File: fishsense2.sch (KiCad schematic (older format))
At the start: 20 parts, among them J1 Conn_02x10_Odd_Even, J2 Screw_Terminal_01x02, J3 Conn_01x02, J4 Conn_01x02, J5 Conn_01x02, J6 USB_C_Receptacle, J7 USB_C_Receptacle, J8 USB_C_Receptacle, K1 ADW11, U1 P783F-Q24-S5-S, U2 AD9951

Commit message: Added symbols and footprints. More space for connectors on PCB.
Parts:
- removed J7, J8: USB_C_Receptacle, Connector_USB:USB_C_Receptacle_GCT_USB4085, symbol Connector:USB_C_Receptacle
- removed U2: AD9951, Package_QFP:TQFP-48-1EP_7x7mm_P0.5mm_EP3.5x3.5mm, symbol Interface:AD9951
- added J7, J8: USB3_A, Connector_USB:USB3_A_Molex_48393-001, symbol Connector:USB3_A
- added U2: TUSB8020BIPHP, fishsense2:TUSB8020BIPHP, symbol New_Library:TUSB8020BIPHP
- added U3: HD3SS3220, fishsense2:TI_VQFN_RNH, symbol New_Library:HD3SS3220
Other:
- moved on the sheet: J3, U1
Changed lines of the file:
@@
 $EndDescr
-$Comp
-L Interface:AD9951 U2
-U 1 1 6166350E
-P 4450 3650
-F 0 "U2" H 5594 3696 50  0000 L CNN
-F 1 "AD9951" H 5594 3605 50  0000 L CNN
-F 2 "Package_QFP:TQFP-48-1EP_7x7mm_P0.5mm_EP3.5x3.5mm" H 4450 2450 50  0001 C CIN
-F 3 "https://www.analog.com/static/imported-files/data_sheets/AD9951.pdf" H 4450 3650 50  0001 C CNN
-	1    4450 3650
-	1    0    0    -1
-$EndComp
-$Comp
-L Connector:USB_C_Receptacle J8
-U 1 1 61664802
-P 9700 2150
-F 0 "J8" H 9807 3417 50  0000 C CNN
-F 1 "USB_C_Receptacle" H 9807 3326 50  0000 C CNN
-F 2 "Connector_USB:USB_C_Receptacle_GCT_USB4085" H 9850 2150 50  0001 C CNN
-F 3 "https://www.usb.org/sites/default/files/documents/usb_type-c.zip" H 9850 2150 50  0001 C CNN
-	1    9700 2150
-	1    0    0    -1
-$EndComp
-$Comp
-L Connector:USB_C_Receptacle J7
-U 1 1 61667CF7
-P 9650 5100
-F 0 "J7" H 9757 6367 50  0000 C CNN
-F 1 "USB_C_Receptacle" H 9757 6276 50  0000 C CNN
-F 2 "Connector_USB:USB_C_Receptacle_GCT_USB4085" H 9800 5100 50  0001 C CNN
-F 3 "https://www.usb.org/sites/default/files/documents/usb_type-c.zip" H 9800 5100 50  0001 C CNN
-	1    9650 5100
-	1    0    0    -1
-$EndComp
-$Comp
-L Connector:USB_C_Receptacle J6
-U 1 1 6166A7B3
-P 8400 5100
-F 0 "J6" H 8507 6367 50  0000 C CNN
-F 1 "USB_C_Receptacle" H 8507 6276 50  0000 C CNN
-F 2 "Connector_USB:USB_C_Receptacle_GCT_USB4085" H 8550 5100 50  0001 C CNN
-F 3 "https://www.usb.org/sites/default/files/documents/usb_type-c.zip" H 8550 5100 50  0001 C CNN
-	1    8400 5100
-	1    0    0    -1
-$EndComp
 $Comp
 L Device:LED D1
@@
 L New_Library:P783F-Q24-S5-S U1
 U 1 1 616833DA
-P 1850 4100
-F 0 "U1" H 2075 4225 50  0000 C CNN
-F 1 "P783F-Q24-S5-S" H 2075 4134 50  0000 C CNN
-F 2 "Converter_DCDC:Converter_DCDC_RECOM_R5xxxPA_THT" H 1850 4100 50  0001 C CNN
-F 3 "" H 1850 4100 50  0001 C CNN
-	1    1850 4100
+P 4750 6050
+F 0 "U1" H 4975 6175 50  0000 C CNN
+F 1 "P783F-Q24-S5-S" H 4975 6084 50  0000 C CNN
+F 2 "Converter_DCDC:Converter_DCDC_RECOM_R5xxxPA_THT" H 4750 6050 50  0001 C CNN
+F 3 "" H 4750 6050 50  0001 C CNN
+	1    4750 6050
 	1    0    0    -1
 $EndComp
@@
 L Relay:ADW11 K1
 U 1 1 6168A988
-P 2800 6200
-F 0 "K1" H 3230 6246 50  0000 L CNN
-F 1 "ADW11" H 3230 6155 50  0000 L CNN
-F 2 "Relay_THT:Relay_SPST_TE_PCN-1xxD3MHZ" H 4125 6150 50  0001 C CNN
-F 3 "https://www.panasonic-electric-works.com/pew/es/downloads/ds_dw_hl_en.pdf" H 2800 6200 50  0001 C CNN
-	1    2800 6200
+P 2250 6900
+F 0 "K1" H 2680 6946 50  0000 L CNN
+F 1 "ADW11" H 2680 6855 50  0000 L CNN
+F 2 "Relay_THT:Relay_SPST_TE_PCN-1xxD3MHZ" H 3575 6850 50  0001 C CNN
+F 3 "https://www.panasonic-electric-works.com/pew/es/downloads/ds_dw_hl_en.pdf" H 2250 6900 50  0001 C CNN
+	1    2250 6900
 	1    0    0    -1
 $EndComp
@@
 L Connector_Generic:Conn_01x02 J3
 U 1 1 616936C7
-P 3150 1900
-F 0 "J3" H 3230 1892 50  0000 L CNN
-F 1 "Conn_01x02" H 3230 1801 50  0000 L CNN
-F 2 "Connector_AMASS:AMASS_XT30U-F_1x02_P5.0mm_Vertical" H 3150 1900 50  0001 C CNN
-F 3 "~" H 3150 1900 50  0001 C CNN
-	1    3150 1900
+P 2950 1650
+F 0 "J3" H 3030 1642 50  0000 L CNN
+F 1 "Conn_01x02" H 3030 1551 50  0000 L CNN
+F 2 "Connector_AMASS:AMASS_XT30U-F_1x02_P5.0mm_Vertical" H 2950 1650 50  0001 C CNN
+F 3 "~" H 2950 1650 50  0001 C CNN
+	1    2950 1650
 	1    0    0    -1
 $EndComp
@@
 	1    0    0    -1
 $EndComp
+$Comp
+L Connector:USB3_A J7
+U 1 1 616E2E2E
+P 9650 2550
+F 0 "J7" H 9707 3267 50  0000 C CNN
+F 1 "USB3_A" H 9707 3176 50  0000 C CNN
+F 2 "Connector_USB:USB3_A_Molex_48393-001" H 9800 2650 50  0001 C CNN
+F 3 "~" H 9800 2650 50  0001 C CNN
+	1    9650 2550
+	1    0    0    -1
+$EndComp
+$Comp
+L Connector:USB3_A J8
+U 1 1 616E6C04
+P 9650 4300
+F 0 "J8" H 9707 5017 50  0000 C CNN
+F 1 "USB3_A" H 9707 4926 50  0000 C CNN
+F 2 "Connector_USB:USB3_A_Molex_48393-001" H 9800 4400 50  0001 C CNN
+F 3 "~" H 9800 4400 50  0001 C CNN
+	1    9650 4300
+	1    0    0    -1
+$EndComp
+$Comp
+L New_Library:HD3SS3220 U3
+U 1 1 61711409
+P 7500 4600
+F 0 "U3" H 7500 5615 50  0000 C CNN
+F 1 "HD3SS3220" H 7500 5524 50  0000 C CNN
+F 2 "fishsense2:TI_VQFN_RNH" H 7500 5550 50  0001 C CNN
+F 3 "" H 7500 5550 50  0001 C CNN
+	1    7500 4600
+	1    0    0    -1
+$EndComp
+$Comp
+L New_Library:TUSB8020BIPHP U2
+U 1 1 61718548
+P 4000 3900
+F 0 "U2" H 4000 5888 60  0000 C CNN
+F 1 "TUSB8020BIPHP" H 4000 5782 60  0000 C CNN
+F 2 "fishsense2:TUSB8020BIPHP" H 4000 4140 60  0001 C CNN
+F 3 "" H 3800 5700 60  0000 C CNN
+	1    4000 3900
+	1    0    0    -1
+$EndComp
+$Comp
+L Connector:USB_C_Receptacle J6
+U 1 1 6172C2EF
+P 1100 4900
+F 0 "J6" H 1207 6167 50  0000 C CNN
+F 1 "USB_C_Receptacle" H 1207 6076 50  0000 C CNN
+F 2 "Connector_USB:USB_C_Receptacle_GCT_USB4085" H 1250 4900 50  0001 C CNN
+F 3 "https://www.usb.org/sites/default/files/documents/usb_type-c.zip" H 1250 4900 50  0001 C CNN
+	1    1100 4900
+	1    0    0    -1
+$EndComp

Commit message: Finished schematic. Added all footprints. Arranged components and routed differential signals.
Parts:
- removed D2, D3, D4: LED, LED_THT:LED_D5.0mm_FlatTop, symbol Device:LED
- removed F1: Fuse, Fuse:Fuseholder_Cylinder-5x20mm_Stelvio-Kontek_PTF78_Horizontal_Open, symbol Device:Fuse
- removed J2: Screw_Terminal_01x02, TerminalBlock:TerminalBlock_Altech_AK300-2_P5.00mm, symbol Connector:Screw_Terminal_01x02
- removed J3: Conn_01x02, Connector_AMASS:AMASS_XT30U-F_1x02_P5.0mm_Vertical, symbol Connector_Generic:Conn_01x02
- removed J4, J5: Conn_01x02, Connector_PinHeader_2.54mm:PinHeader_1x02_P2.54mm_Vertical, symbol Connector_Generic:Conn_01x02
- removed K1: ADW11, Relay_THT:Relay_SPST_TE_PCN-1xxD3MHZ, symbol Relay:ADW11
- removed U1: P783F-Q24-S5-S, Converter_DCDC:Converter_DCDC_RECOM_R5xxxPA_THT, symbol New_Library:P783F-Q24-S5-S
- added C1, C4: 18p, Capacitor_SMD:C_0603_1608Metric, symbol Device:C
- added C10, C12, C13, C14, C15, C21: 100n, Capacitor_SMD:C_0402_1005Metric, symbol Device:C
- added C11, C16, C17, C19, C2, C20, C22, C23, C3, C35, C36, C37, C38, C5, C6, C7, C8, C9: 0.1u, Capacitor_SMD:C_0402_1005Metric, symbol Device:C
- added C18: 10u, Capacitor_SMD:C_1206_3216Metric, symbol Device:C
- added C24: 100u, Capacitor_THT:CP_Radial_D5.0mm_P2.00mm, symbol Device:CP1
- added C25: 1u, Capacitor_SMD:C_1206_3216Metric, symbol Device:C
- added Q1: Q_NMOS_DGS, Package_TO_SOT_SMD:SOT-23, symbol Device:Q_NMOS_DGS
- added R1: 1M, Resistor_SMD:R_0603_1608Metric, symbol Device:R_US
- added R2: 90k, Resistor_SMD:R_0603_1608Metric, symbol Device:R_US
- added R3: 10k, Resistor_SMD:R_0603_1608Metric, symbol Device:R_US
- added R4: 9k53, Resistor_SMD:R_0603_1608Metric, symbol Device:R_US
- added R5: 200k, Resistor_SMD:R_0603_1608Metric, symbol Device:R_US
- added R6: 4.7k, Resistor_SMD:R_0603_1608Metric, symbol Device:R_US
- added R7: 900k, Resistor_SMD:R_0603_1608Metric, symbol Device:R_US
- added R8: 1k, Resistor_SMD:R_0603_1608Metric, symbol Device:R_US
- added R9: 220, Resistor_SMD:R_0603_1608Metric, symbol Device:R_US
- added SW1: SW_Reed, Connector_JST:JST_PH_B2B-PH-K_1x02_P2.00mm_Vertical, symbol Switch:SW_Reed
- added TP1: CC1, TestPoint:TestPoint_Pad_1.5x1.5mm, symbol Connector:TestPoint
- added TP2: CC2, TestPoint:TestPoint_Pad_1.5x1.5mm, symbol Connector:TestPoint
- added Y1: Crystal, Crystal:Crystal_SMD_0603-2Pin_6.0x3.5mm, symbol Device:Crystal
- J6: footprint Connector_USB:USB_C_Receptacle_GCT_USB4085 -> Connector_USB:USB_C_Receptacle_JAE_DX07S024WJ1R350
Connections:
- net labels added: +3.3V, +5V, CC1, CC2, D_DN1_N, D_DN1_P, D_DN2_N, D_DN2_P, D_UP_N, D_UP_P, GND, REED, RELAY_CTL, RX1_N, RX1_P, RX2_N, RX2_P, RX_DN1_N, RX_DN1_P, RX_DN2_N, RX_DN2_P, RX_N, RX_P, TX1_F_N, TX1_F_P, TX1_N, TX1_P, TX2_F_N, TX2_F_P, TX2_N, TX2_P, TX_DN1_F_N, TX_DN1_F_P, TX_DN1_N, TX_DN1_P, TX_DN2_F_N, TX_DN2_F_P, TX_DN2_N, TX_DN2_P, TX_N, TX_P, VBUS_UP, XI, XO
- wire segments 0 -> 241
- no-connect marks 0 -> 30
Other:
- note added: "Orbitty Connector"
- note added: "USB Hub"
- note added: "USB Receptacles"
- moved on the sheet: D1, H1, H2, H3, H4, J1, J7, J8

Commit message: Updated footprints. Placed components and added silkscreen.
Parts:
- removed C1, C4: 18p, Capacitor_SMD:C_0603_1608Metric, symbol Device:C
- removed C10, C12, C13, C14, C15, C21: 100n, Capacitor_SMD:C_0402_1005Metric, symbol Device:C
- removed C11, C16, C17, C19, C2, C20, C22, C23, C3, C35, C36, C37, C38, C5, C6, C7, C8, C9: 0.1u, Capacitor_SMD:C_0402_1005Metric, symbol Device:C
- removed C18: 10u, Capacitor_SMD:C_1206_3216Metric, symbol Device:C
- removed C24: 100u, Capacitor_THT:CP_Radial_D5.0mm_P2.00mm, symbol Device:CP1
- removed C25: 1u, Capacitor_SMD:C_1206_3216Metric, symbol Device:C
- removed J6: USB_C_Receptacle, Connector_USB:USB_C_Receptacle_JAE_DX07S024WJ1R350, symbol Connector:USB_C_Receptacle
- removed R1: 1M, Resistor_SMD:R_0603_1608Metric, symbol Device:R_US
- removed R2: 90k, Resistor_SMD:R_0603_1608Metric, symbol Device:R_US
- removed R3: 10k, Resistor_SMD:R_0603_1608Metric, symbol Device:R_US
- removed R4: 9k53, Resistor_SMD:R_0603_1608Metric, symbol Device:R_US
- removed R5: 200k, Resistor_SMD:R_0603_1608Metric, symbol Device:R_US
- removed R6: 4.7k, Resistor_SMD:R_0603_1608Metric, symbol Device:R_US
- removed R7: 900k, Resistor_SMD:R_0603_1608Metric, symbol Device:R_US
- removed R8: 1k, Resistor_SMD:R_0603_1608Metric, symbol Device:R_US
- removed TP1: CC1, TestPoint:TestPoint_Pad_1.5x1.5mm, symbol Connector:TestPoint
- removed TP2: CC2, TestPoint:TestPoint_Pad_1.5x1.5mm, symbol Connector:TestPoint
- removed U2: TUSB8020BIPHP, fishsense2:TUSB8020BIPHP, symbol New_Library:TUSB8020BIPHP
- removed U3: HD3SS3220, fishsense2:TI_VQFN_RNH, symbol New_Library:HD3SS3220
- removed Y1: Crystal, Crystal:Crystal_SMD_0603-2Pin_6.0x3.5mm, symbol Device:Crystal
- added J10: USB_B_Micro, Connector_USB:USB_Micro-B_GCT_USB3076-30-A, symbol Connector:USB_B_Micro
- added J5, J6: USB3_A, Connector_USB:USB3_A_Molex_48393-001, symbol Connector:USB3_A
- added J9: Barrel_Jack, Connector_BarrelJack:BarrelJack_Horizontal, symbol Connector:Barrel_Jack
- R9: footprint Resistor_SMD:R_0603_1608Metric -> Resistor_SMD:R_1206_3216Metric_Pad1.30x1.75mm_HandSolder
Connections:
- net labels removed: +3.3V, +5V, CC1, CC2, D_DN1_N, D_DN1_P, D_DN2_N, D_DN2_P, D_UP_N, D_UP_P, RX1_N, RX1_P, RX2_N, RX2_P, RX_DN1_N, RX_DN1_P, RX_DN2_N, RX_DN2_P, RX_N, RX_P, TX1_F_N, TX1_F_P, TX1_N, TX1_P, TX2_F_N, TX2_F_P, TX2_N, TX2_P, TX_DN1_F_N, TX_DN1_F_P, TX_DN1_N, TX_DN1_P, TX_DN2_F_N, TX_DN2_F_P, TX_DN2_N, TX_DN2_P, TX_N, TX_P, VBUS_UP, XI, XO
- wire segments 241 -> 14
- no-connect marks 30 -> 11
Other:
- note removed: "USB Hub"
- note removed: "USB Receptacles"
- moved on the sheet: D1, H1, H2, H3, H4, J1, Q1, R9, SW1

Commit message: Changed footprints to right angle versions. Adjusted board outline to orbitty carrier size.
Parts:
- SW1: footprint Connector_JST:JST_PH_B2B-PH-K_1x02_P2.00mm_Vertical -> Connector_JST:JST_PH_S2B-PH-K_1x02_P2.00mm_Horizontal
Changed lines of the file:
@@
 F 0 "SW1" V 1896 4365 50  0000 R CNN
 F 1 "SW_Reed" V 1805 4365 50  0000 R CNN
-F 2 "Connector_JST:JST_PH_B2B-PH-K_1x02_P2.00mm_Vertical" H 1850 4450 50  0001 C CNN
+F 2 "Connector_JST:JST_PH_S2B-PH-K_1x02_P2.00mm_Horizontal" H 1850 4450 50  0001 C CNN
 F 3 "~" H 1850 4450 50  0001 C CNN
 	1    1850 4450

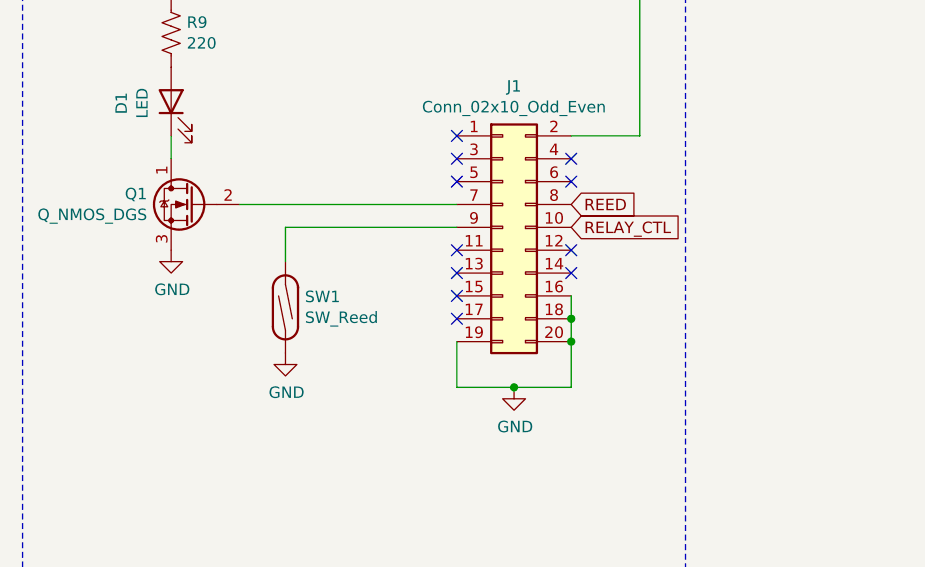
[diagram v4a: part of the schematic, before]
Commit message: Removed uneeded DC barrel power. Adjusted component values for 12v supply. Checked footprints.
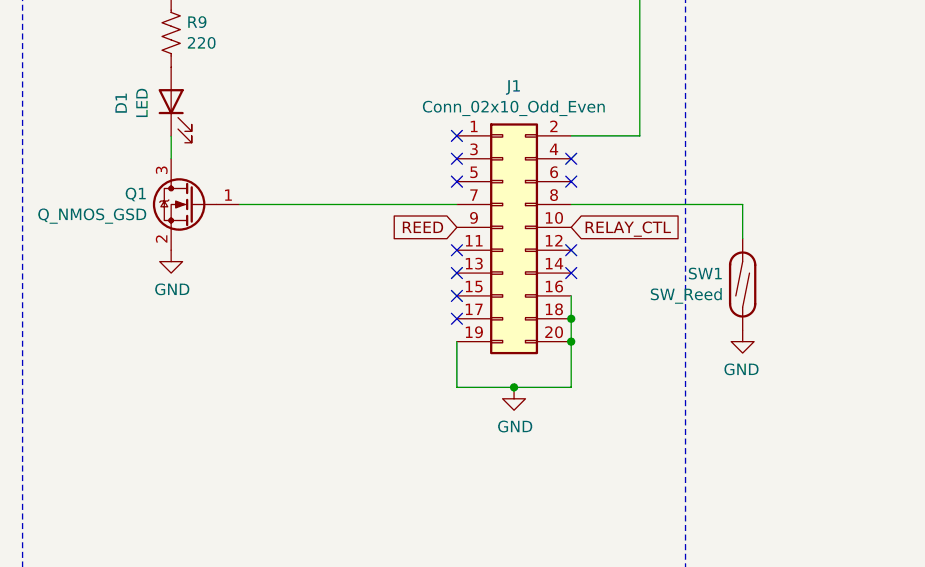
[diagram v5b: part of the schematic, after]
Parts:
- removed Q1: Q_NMOS_DGS, Package_TO_SOT_SMD:SOT-23, symbol Device:Q_NMOS_DGS
- added Q1: Q_NMOS_GSD, Package_TO_SOT_SMD:SOT-23_Handsoldering, symbol Device:Q_NMOS_GSD
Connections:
- net GND: now also Q1.2 (S)
- net REED: now also J1.9 (Pin_9); no longer J1.8 (Pin_8)
- net at D1.1 (K): now also Q1.3 (D)
- net at J1.7 (Pin_7): now also Q1.1 (G)
- net at SW1.2: now also J1.8 (Pin_8); no longer J1.9 (Pin_9)
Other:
- moved on the sheet: SW1
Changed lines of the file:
@@
 NoConn ~ 2600 4400
 NoConn ~ 2600 4500
-Text GLabel 3100 4000 2    50   Input ~ 0
+Text GLabel 2600 4100 0    50   Input ~ 0
 REED
 Text GLabel 3100 4100 2    50   Input ~ 0
@@
 L Switch:SW_Reed SW1
 U 1 1 622296A5
-P 1850 4450
-F 0 "SW1" V 1896 4365 50  0000 R CNN
-F 1 "SW_Reed" V 1805 4365 50  0000 R CNN
-F 2 "Connector_JST:JST_PH_S2B-PH-K_1x02_P2.00mm_Horizontal" H 1850 4450 50  0001 C CNN
-F 3 "~" H 1850 4450 50  0001 C CNN
-	1    1850 4450
-	0    -1   -1   0
+P 3850 4350
+F 0 "SW1" V 3896 4265 50  0000 R CNN
+F 1 "SW_Reed" V 3805 4265 50  0000 R CNN
+F 2 "Connector_JST:JST_PH_S2B-PH-K_1x02_P2.00mm_Horizontal" H 3850 4350 50  0001 C CNN
+F 3 "~" H 3850 4350 50  0001 C CNN
+	1    3850 4350
+	0    1    -1   0
 $EndComp
 $Comp
 L power:GND #PWR0128
 U 1 1 6222A48E
-P 1850 4650
-F 0 "#PWR0128" H 1850 4400 50  0001 C CNN
-F 1 "GND" H 1855 4477 50  0000 C CNN
-F 2 "" H 1850 4650 50  0001 C CNN
-F 3 "" H 1850 4650 50  0001 C CNN
-	1    1850 4650
-	1    0    0    -1
+P 3850 4550
+F 0 "#PWR0128" H 3850 4300 50  0001 C CNN
+F 1 "GND" H 3855 4377 50  0000 C CNN
+F 2 "" H 3850 4550 50  0001 C CNN
+F 3 "" H 3850 4550 50  0001 C CNN
+	1    3850 4550
+	-1   0    0    -1
 $EndComp
 Wire Wire Line
-	2600 4100 1850 4100
+	3100 4000 3850 4000
 Wire Wire Line
-	1850 4100 1850 4250
-$Comp
-L Device:Q_NMOS_DGS Q1
-U 1 1 62260F2D
-P 1450 4000
-F 0 "Q1" H 1655 4046 50  0000 L CNN
-F 1 "Q_NMOS_DGS" H 1655 3955 50  0000 L CNN
-F 2 "Package_TO_SOT_SMD:SOT-23" H 1650 4100 50  0001 C CNN
-F 3 "~" H 1450 4000 50  0001 C CNN
-	1    1450 4000
-	-1   0    0    -1
-$EndComp
+	3850 4000 3850 4150
 Wire Wire Line
 	2600 4000 1650 4000
@@
 	1    0    0    -1
 $EndComp
+$Comp
+L Device:Q_NMOS_GSD Q1
+U 1 1 619E7610
+P 1450 4000
+F 0 "Q1" H 1655 4046 50  0000 L CNN
+F 1 "Q_NMOS_GSD" H 1655 3955 50  0000 L CNN
+F 2 "Package_TO_SOT_SMD:SOT-23_Handsoldering" H 1650 4100 50  0001 C CNN
+F 3 "~" H 1450 4000 50  0001 C CNN
+	1    1450 4000
+	-1   0    0    -1
+$EndComp
 $EndSCHEMATC

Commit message: Routed traces.
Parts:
- removed J10: USB_B_Micro, Connector_USB:USB_Micro-B_GCT_USB3076-30-A, symbol Connector:USB_B_Micro
- removed J5, J6, J7, J8: USB3_A, Connector_USB:USB3_A_Molex_48393-001, symbol Connector:USB3_A
- removed J9: Barrel_Jack, Connector_BarrelJack:BarrelJack_Horizontal, symbol Connector:Barrel_Jack
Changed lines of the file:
@@
 	11250 1900 4650 1900
-$Comp
-L Connector:USB3_A J5
-U 1 1 6196CE86
-P 5600 2900
-F 0 "J5" H 5657 3617 50  0000 C CNN
-F 1 "USB3_A" H 5657 3526 50  0000 C CNN
-F 2 "Connector_USB:USB3_A_Molex_48393-001" H 5750 3000 50  0001 C CNN
-F 3 "~" H 5750 3000 50  0001 C CNN
-	1    5600 2900
-	1    0    0    -1
-$EndComp
-$Comp
-L Connector:USB3_A J6
-U 1 1 6196EAC1
-P 5600 4400
-F 0 "J6" H 5657 5117 50  0000 C CNN
-F 1 "USB3_A" H 5657 5026 50  0000 C CNN
-F 2 "Connector_USB:USB3_A_Molex_48393-001" H 5750 4500 50  0001 C CNN
-F 3 "~" H 5750 4500 50  0001 C CNN
-	1    5600 4400
-	1    0    0    -1
-$EndComp
-$Comp
-L Connector:USB3_A J7
-U 1 1 619702D6
-P 5600 5900
-F 0 "J7" H 5657 6617 50  0000 C CNN
-F 1 "USB3_A" H 5657 6526 50  0000 C CNN
-F 2 "Connector_USB:USB3_A_Molex_48393-001" H 5750 6000 50  0001 C CNN
-F 3 "~" H 5750 6000 50  0001 C CNN
-	1    5600 5900
-	1    0    0    -1
-$EndComp
-$Comp
-L Connector:USB3_A J8
-U 1 1 619726A9
-P 5600 7450
-F 0 "J8" H 5657 8167 50  0000 C CNN
-F 1 "USB3_A" H 5657 8076 50  0000 C CNN
-F 2 "Connector_USB:USB3_A_Molex_48393-001" H 5750 7550 50  0001 C CNN
-F 3 "~" H 5750 7550 50  0001 C CNN
-	1    5600 7450
-	1    0    0    -1
-$EndComp
-$Comp
-L Connector:Barrel_Jack J9
-U 1 1 61974C09
-P 8300 3350
-F 0 "J9" H 8357 3675 50  0000 C CNN
-F 1 "Barrel_Jack" H 8357 3584 50  0000 C CNN
-F 2 "Connector_BarrelJack:BarrelJack_Horizontal" H 8350 3310 50  0001 C CNN
-F 3 "~" H 8350 3310 50  0001 C CNN
-	1    8300 3350
-	1    0    0    -1
-$EndComp
-$Comp
-L Connector:USB_B_Micro J10
-U 1 1 619775BF
-P 8300 4400
-F 0 "J10" H 8357 4867 50  0000 C CNN
-F 1 "USB_B_Micro" H 8357 4776 50  0000 C CNN
-F 2 "Connector_USB:USB_Micro-B_GCT_USB3076-30-A" H 8450 4350 50  0001 C CNN
-F 3 "~" H 8450 4350 50  0001 C CNN
-	1    8300 4400
-	1    0    0    -1
-$EndComp
 $Comp
 L Device:Q_NMOS_GSD Q1

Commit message: Some footprint and part changes based on availability.
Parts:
- SW1: footprint Connector_JST:JST_PH_S2B-PH-K_1x02_P2.00mm_Horizontal -> Connector_JST:JST_XH_S2B-XH-A_1x02_P2.50mm_Horizontal
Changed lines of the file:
@@
 F 0 "SW1" V 3896 4265 50  0000 R CNN
 F 1 "SW_Reed" V 3805 4265 50  0000 R CNN
-F 2 "Connector_JST:JST_PH_S2B-PH-K_1x02_P2.00mm_Horizontal" H 3850 4350 50  0001 C CNN
+F 2 "Connector_JST:JST_XH_S2B-XH-A_1x02_P2.50mm_Horizontal" H 3850 4350 50  0001 C CNN
 F 3 "~" H 3850 4350 50  0001 C CNN
 	1    3850 4350
